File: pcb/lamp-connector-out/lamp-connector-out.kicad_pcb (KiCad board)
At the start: 2 copper layers, 41.1 x 28.9 mm, 2 parts

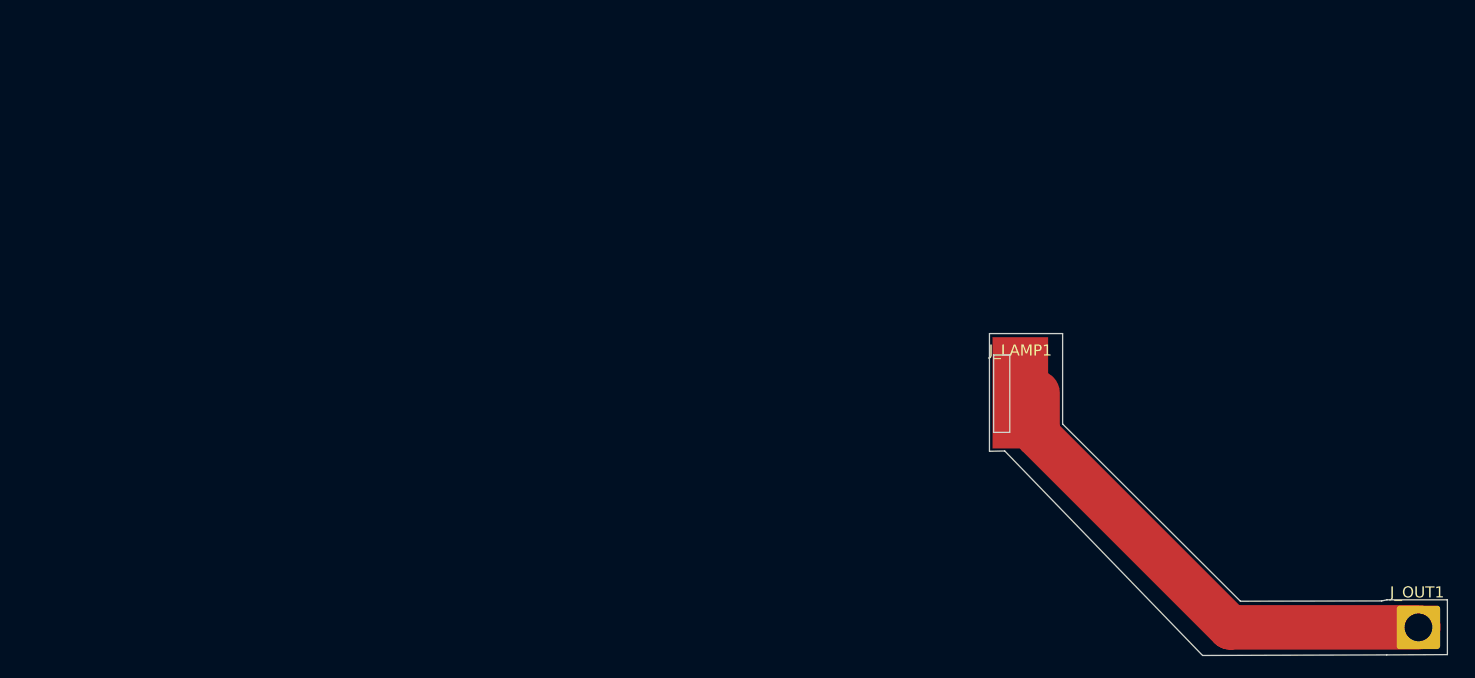
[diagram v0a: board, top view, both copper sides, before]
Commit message: Updated with correct measurements and G43.* behaviour
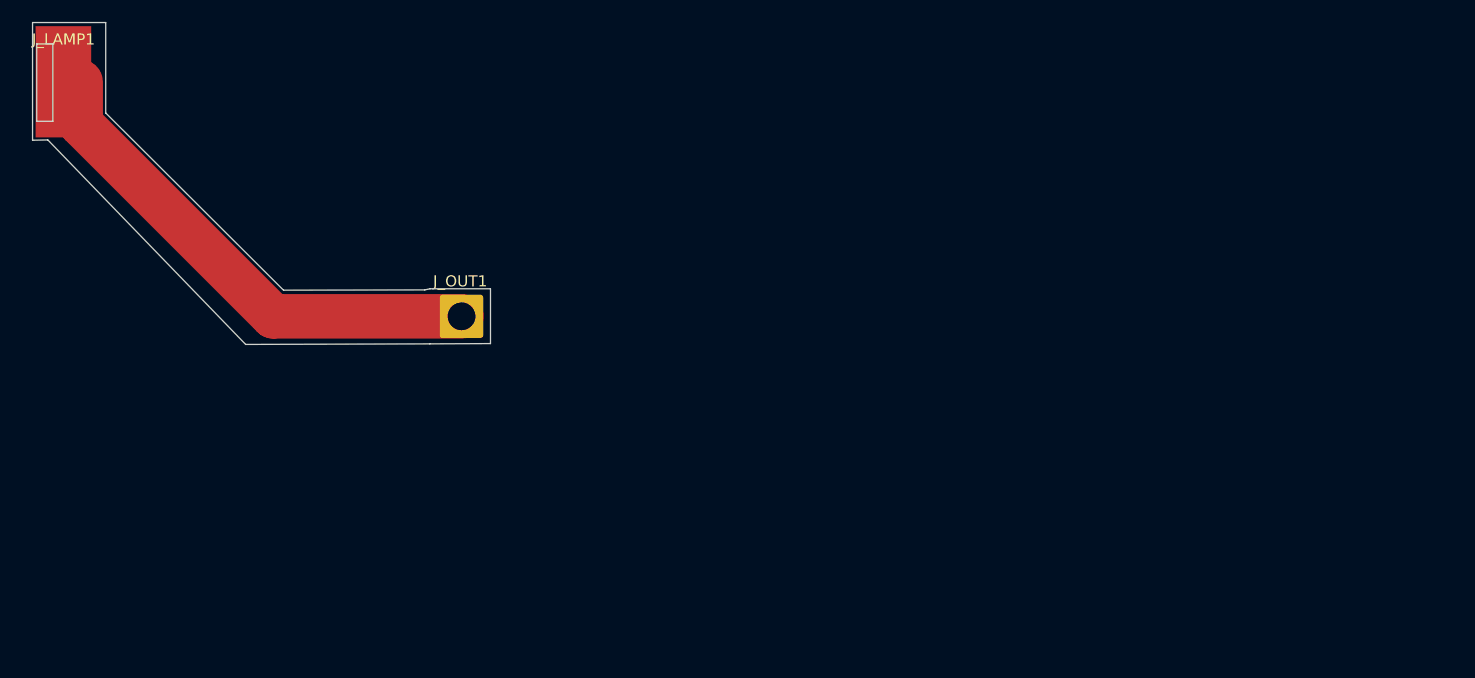
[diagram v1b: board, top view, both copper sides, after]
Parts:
- moved J_OUT1 90.4 mm to (38.8, 26.5)
- moved J_LAMP1 90.4 mm to (3.19, 5.42)
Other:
- outline, holes or cut-outs redrawn
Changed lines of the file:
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@@
 		(pad_to_mask_clearance 0)
 		(allow_soldermask_bridges_in_footprints no)
+		(grid_origin 0.5 29.1)
 		(pcbplotparams
-			(layerselection 0x00010fc_ffffffff)
+			(layerselection 0x0001000_7fffffff)
 			(plot_on_all_layers_selection 0x0000000_00000000)
 			(disableapertmacros no)
@@
 			(usegerberattributes yes)
 			(usegerberadvancedattributes yes)
-			(creategerberjobfile yes)
+			(creategerberjobfile no)
 			(dashed_line_dash_ratio 12.000000)
 			(dashed_line_gap_ratio 3.000000)
@@
 			(viasonmask no)
 			(mode 1)
-			(useauxorigin no)
+			(useauxorigin yes)
 			(hpglpennumber 1)
 			(hpglpenspeed 20)
@@
 			(outputformat 1)
 			(mirror no)
-			(drillshape 1)
+			(drillshape 0)
 			(scaleselection 1)
 			(outputdirectory "")
@@
 	(footprint "Connector_Wire:SolderWirePad_1x01_SMD_5x10mm"
 		(layer "F.Cu")
-		(at 89.175 33.375)
+		(at 3.1875 5.425)
 		(descr "Wire Pad, Square, SMD Pad,  5mm x 10mm,")
 		(tags "MesurementPoint Square SMDPad 5mmx10mm ")
@@
 	(footprint "Connector_Wire:SolderWire-2sqmm_1x01_D2mm_OD3.9mm"
 		(layer "F.Cu")
-		(at 124.825 54.45)
+		(at 38.8375 26.5)
 		(descr "Soldered wire connection, for a single 2 mm² wire, reinforced insulation, conductor diameter 2mm, outer diameter 3.9mm, size source Multi-Contact FLEXI-xV 2.0 (https://ec.staubli.com/AcroFiles/Catalogues/TM_Cab-Main-11014119_(en)_hi.pdf), bend radius 3 times outer diameter, generated with kicad-footprint-generator")
 		(tags "connector wire 2sqmm")
@@
 	(gr_poly
 		(pts
-			(xy 125.005988 53.559798) (xy 125.061988 53.564998) (xy 125.116988 53.573798) (xy 125.171988 53.585998)
-			(xy 125.225989 53.601699) (xy 125.277991 53.620597) (xy 125.329993 53.642898) (xy 125.379988 53.6683)
-			(xy 125.427992 53.696898) (xy 125.47399 53.728297) (xy 125.518988 53.762698) (xy 125.560988 53.7998)
-			(xy 125.59999 53.839396) (xy 125.636992 53.8814) (xy 125.671988 53.9257) (xy 125.702994 53.971999)
-			(xy 125.731993 54.020297) (xy 125.756995 54.070197) (xy 125.77899 54.1216) (xy 125.797988 54.174296)
-			(xy 125.813994 54.228198) (xy 125.825987 54.282798) (xy 125.83499 54.338199) (xy 125.839987 54.394)
-			(xy 125.841994 54.45) (xy 125.839987 54.506) (xy 125.83499 54.561797) (xy 125.825987 54.617099) (xy 125.813994 54.671798)
-			(xy 125.797988 54.725596) (xy 125.77899 54.778399) (xy 125.756995 54.829799) (xy 125.731993 54.879699)
-			(xy 125.702994 54.927897) (xy 125.671988 54.974299) (xy 125.636992 55.018599) (xy 125.59999 55.060599)
-			(xy 125.560988 55.1002) (xy 125.518988 55.137298) (xy 125.47399 55.171599) (xy 125.427992 55.203097)
-			(xy 125.379988 55.2317) (xy 125.329993 55.257098) (xy 125.277991 55.279399) (xy 125.225989 55.298297)
-			(xy 125.171988 55.313998) (xy 125.116988 55.326198) (xy 125.061988 55.334998) (xy 125.005988 55.340198)
-			(xy 124.949988 55.341998) (xy 124.893988 55.340198) (xy 124.837989 55.334998) (xy 124.782988 55.326198)
-			(xy 124.727988 55.313998) (xy 124.673995 55.298297) (xy 124.621993 55.279399) (xy 124.569991 55.257098)
-			(xy 124.519988 55.2317) (xy 124.471991 55.203097) (xy 124.425994 55.171599) (xy 124.380988 55.137298)
-			(xy 124.338988 55.1002) (xy 124.299994 55.060599) (xy 124.262992 55.018599) (xy 124.227988 54.974299)
-			(xy 124.19699 54.927897) (xy 124.16799 54.879699) (xy 124.142989 54.829799) (xy 124.120993 54.778399)
-			(xy 124.101988 54.725596) (xy 124.08599 54.671798) (xy 124.073989 54.617099) (xy 124.064994 54.561797)
-			(xy 124.059989 54.506) (xy 124.05799 54.45) (xy 124.059989 54.394) (xy 124.064994 54.338199) (xy 124.073989 54.282798)
-			(xy 124.08599 54.228198) (xy 124.101988 54.174296) (xy 124.120993 54.1216) (xy 124.142989 54.070197)
-			(xy 124.16799 54.020297) (xy 124.19699 53.971999) (xy 124.227988 53.9257) (xy 124.262992 53.8814)
-			(xy 124.299994 53.839396) (xy 124.338988 53.7998) (xy 124.380988 53.762698) (xy 124.425994 53.728297)
-			(xy 124.471991 53.696898) (xy 124.519988 53.6683) (xy 124.569991 53.642898) (xy 124.621993 53.620597)
-			(xy 124.673995 53.601699) (xy 124.727988 53.585998) (xy 124.782988 53.573798) (xy 124.837989 53.564998)
-			(xy 124.893988 53.559798) (xy 124.949988 53.557998)
+			(xy 39.018488 25.609798) (xy 39.074488 25.614998) (xy 39.129488 25.623798) (xy 39.184488 25.635998)
+			(xy 39.238489 25.651699) (xy 39.290491 25.670597) (xy 39.342493 25.692898) (xy 39.392488 25.7183)
+			(xy 39.440492 25.746898) (xy 39.48649 25.778297) (xy 39.531488 25.812698) (xy 39.573488 25.8498)
+			(xy 39.61249 25.889396) (xy 39.649492 25.9314) (xy 39.684488 25.9757) (xy 39.715494 26.021999) (xy 39.744493 26.070297)
+			(xy 39.769495 26.120197) (xy 39.79149 26.1716) (xy 39.810488 26.224296) (xy 39.826494 26.278198)
+			(xy 39.838487 26.332798) (xy 39.84749 26.388199) (xy 39.852487 26.444) (xy 39.854494 26.5) (xy 39.852487 26.556)
+			(xy 39.84749 26.611797) (xy 39.838487 26.667099) (xy 39.826494 26.721798) (xy 39.810488 26.775596)
+			(xy 39.79149 26.828399) (xy 39.769495 26.879799) (xy 39.744493 26.929699) (xy 39.715494 26.977897)
+			(xy 39.684488 27.024299) (xy 39.649492 27.068599) (xy 39.61249 27.110599) (xy 39.573488 27.1502)
+			(xy 39.531488 27.187298) (xy 39.48649 27.221599) (xy 39.440492 27.253097) (xy 39.392488 27.2817)
+			(xy 39.342493 27.307098) (xy 39.290491 27.329399) (xy 39.238489 27.348297) (xy 39.184488 27.363998)
+			(xy 39.129488 27.376198) (xy 39.074488 27.384998) (xy 39.018488 27.390198) (xy 38.962488 27.391998)
+			(xy 38.906488 27.390198) (xy 38.850489 27.384998) (xy 38.795488 27.376198) (xy 38.740488 27.363998)
+			(xy 38.686495 27.348297) (xy 38.634493 27.329399) (xy 38.582491 27.307098) (xy 38.532488 27.2817)
+			(xy 38.484491 27.253097) (xy 38.438494 27.221599) (xy 38.393488 27.187298) (xy 38.351488 27.1502)
+			(xy 38.312494 27.110599) (xy 38.275492 27.068599) (xy 38.240488 27.024299) (xy 38.20949 26.977897)
+			(xy 38.18049 26.929699) (xy 38.155489 26.879799) (xy 38.133493 26.828399) (xy 38.114488 26.775596)
+			(xy 38.09849 26.721798) (xy 38.086489 26.667099) (xy 38.077494 26.611797) (xy 38.072489 26.556) (xy 38.07049 26.5)
+			(xy 38.072489 26.444) (xy 38.077494 26.388199) (xy 38.086489 26.332798) (xy 38.09849 26.278198) (xy 38.114488 26.224296)
+			(xy 38.133493 26.1716) (xy 38.155489 26.120197) (xy 38.18049 26.070297) (xy 38.20949 26.021999) (xy 38.240488 25.9757)
+			(xy 38.275492 25.9314) (xy 38.312494 25.889396) (xy 38.351488 25.8498) (xy 38.393488 25.812698) (xy 38.438494 25.778297)
+			(xy 38.484491 25.746898) (xy 38.532488 25.7183) (xy 38.582491 25.692898) (xy 38.634493 25.670597)
+			(xy 38.686495 25.651699) (xy 38.740488 25.635998) (xy 38.795488 25.623798) (xy 38.850489 25.614998)
+			(xy 38.906488 25.609798) (xy 38.962488 25.607998)
 		)
 		(stroke
@@
 	(gr_poly
 		(pts
-			(xy 87.9 36.6) (xy 87.099997 36.6) (xy 87.099997 30.300002) (xy 87.9 30.300002)
+			(xy 1.9125 8.65) (xy 1.112497 8.65) (xy 1.112497 2.350002) (xy 1.9125 2.350002)
 		)
 		(stroke
@@
 	(gr_poly
 		(pts
-			(xy 87.775 38.6) (xy 86.4 38.625) (xy 86.4 28.05) (xy 92.975 28.05) (xy 92.975 36.175) (xy 108.95 52.1)
-			(xy 121.65 52.075) (xy 122.125 51.975) (xy 127.55 51.975) (xy 127.55 56.9) (xy 122.1 56.925) (xy 105.55 56.975)
+			(xy 1.7875 10.65) (xy 0.4125 10.675) (xy 0.4125 0.1) (xy 6.9875 0.1) (xy 6.9875 8.225) (xy 22.9625 24.15)
+			(xy 35.6625 24.125) (xy 36.1375 24.025) (xy 41.5625 24.025) (xy 41.5625 28.95) (xy 36.1125 28.975)
+			(xy 19.5625 29.025)
 		)
 		(stroke
@@
 	)
 	(gr_rect
-		(start 86.775 29.975)
-		(end 88.225 36.925)
+		(start 0.7875 2.025)
+		(end 2.2375 8.975)
 		(stroke
 			(width 0.05)
@@
 	)
 	(gr_rect
-		(start 86.75 29.95)
-		(end 88.25 36.95)
+		(start 0.7625 2)
+		(end 2.2625 9)
 		(stroke
 			(width 0.1)
@@
 		(layer "Dwgs.User")
 		(pts
-			(xy 125.839987 54.506) (xy 124.059989 54.506)
+			(xy 39.852487 26.556) (xy 38.072489 26.556)
 		)
 		(height 6.181)
 		(gr_text "1.7800 mm"
-			(at 124.949988 47.175 0)
+			(at 38.962488 19.225 0)
 			(layer "Dwgs.User")
 			(effects
@@
 		(layer "Dwgs.User")
 		(pts
-			(xy 124.949988 55.341998) (xy 124.949988 53.557998)
+			(xy 38.962488 27.391998) (xy 38.962488 25.607998)
 		)
 		(height 7.850012)
 		(gr_text "1.7840 mm"
-			(at 131.65 54.449998 90)
+			(at 45.6625 26.499998 90)
 			(layer "Dwgs.User")
 			(effects
@@
 	)
 	(segment
-		(start 90.725 37.15)
-		(end 90.725 33.375)
+		(start 4.7375 9.2)
+		(end 4.7375 5.425)
 		(width 4)
 		(layer "F.Cu")
@@
 	)
 	(segment
-		(start 124.95 54.45)
-		(end 108.025 54.45)
+		(start 38.9625 26.5)
+		(end 22.0375 26.5)
 		(width 4)
 		(layer "F.Cu")
@@
 	)
 	(segment
-		(start 108.025 54.45)
-		(end 90.725 37.15)
+		(start 22.0375 26.5)
+		(end 4.7375 9.2)
 		(width 4)
 		(layer "F.Cu")
